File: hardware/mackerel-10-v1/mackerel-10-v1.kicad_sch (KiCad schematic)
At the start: 24 parts, among them J1 Conn_02x05_Odd_Even, U1 68010D, X1 50 MHz

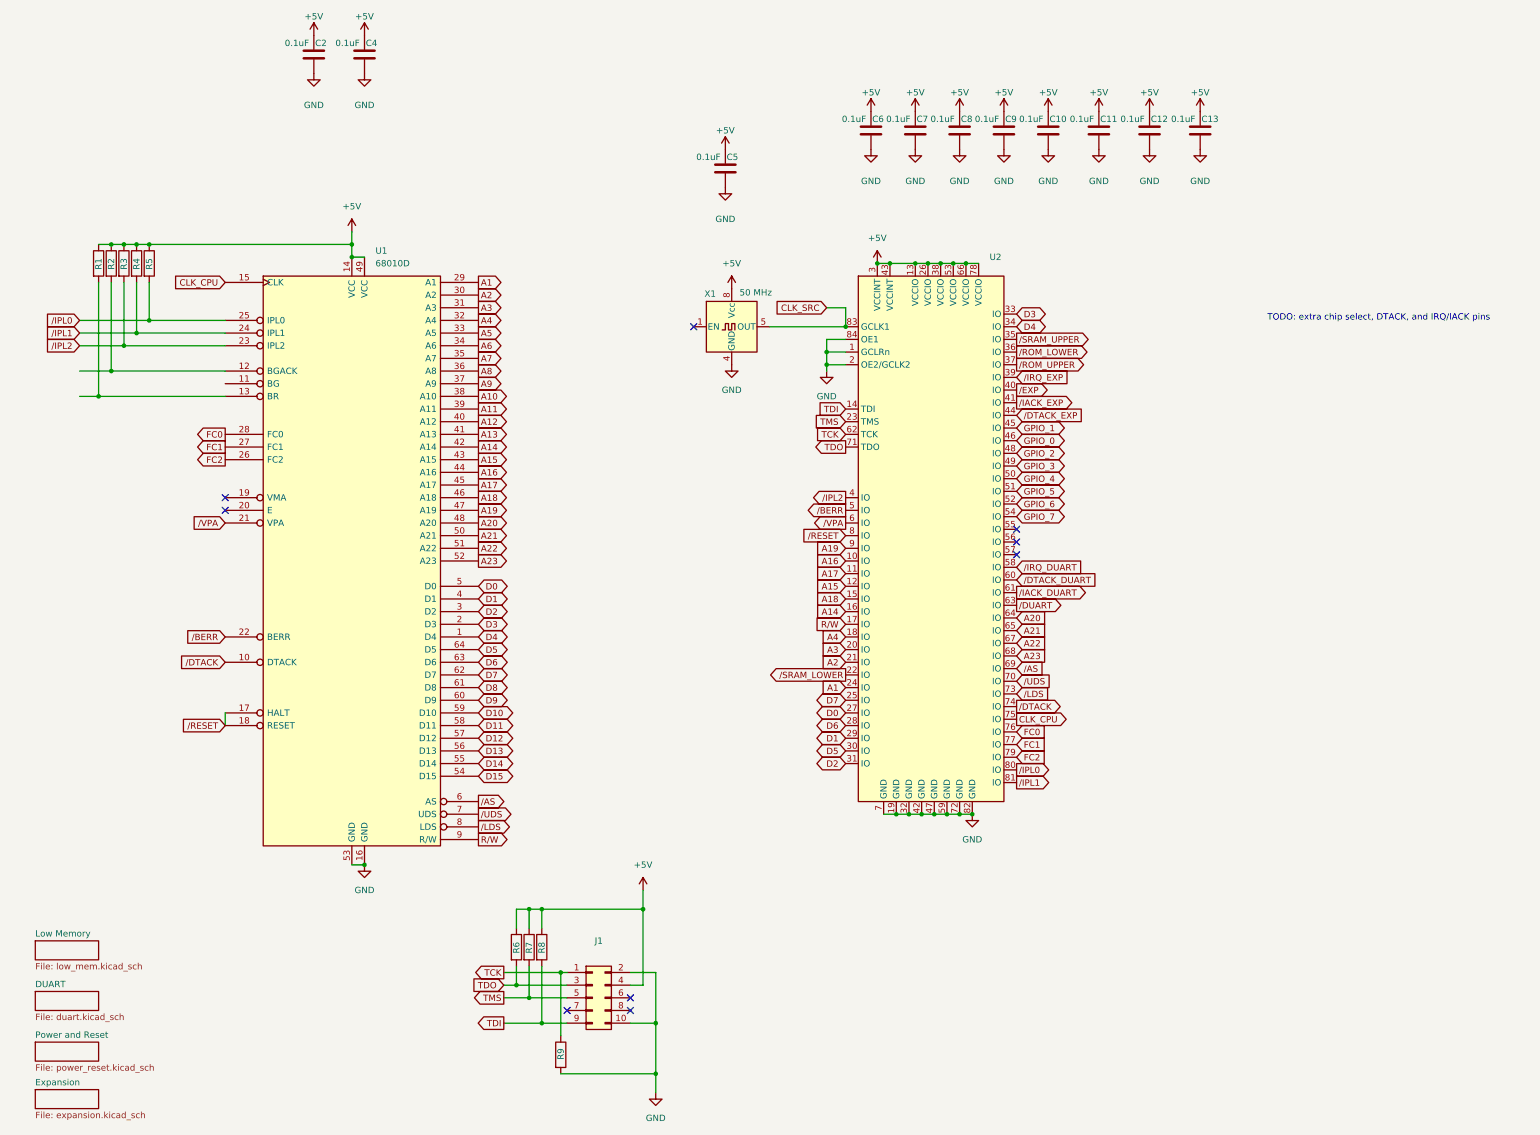
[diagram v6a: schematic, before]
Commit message: Mack-10 proto routed and passing DRC
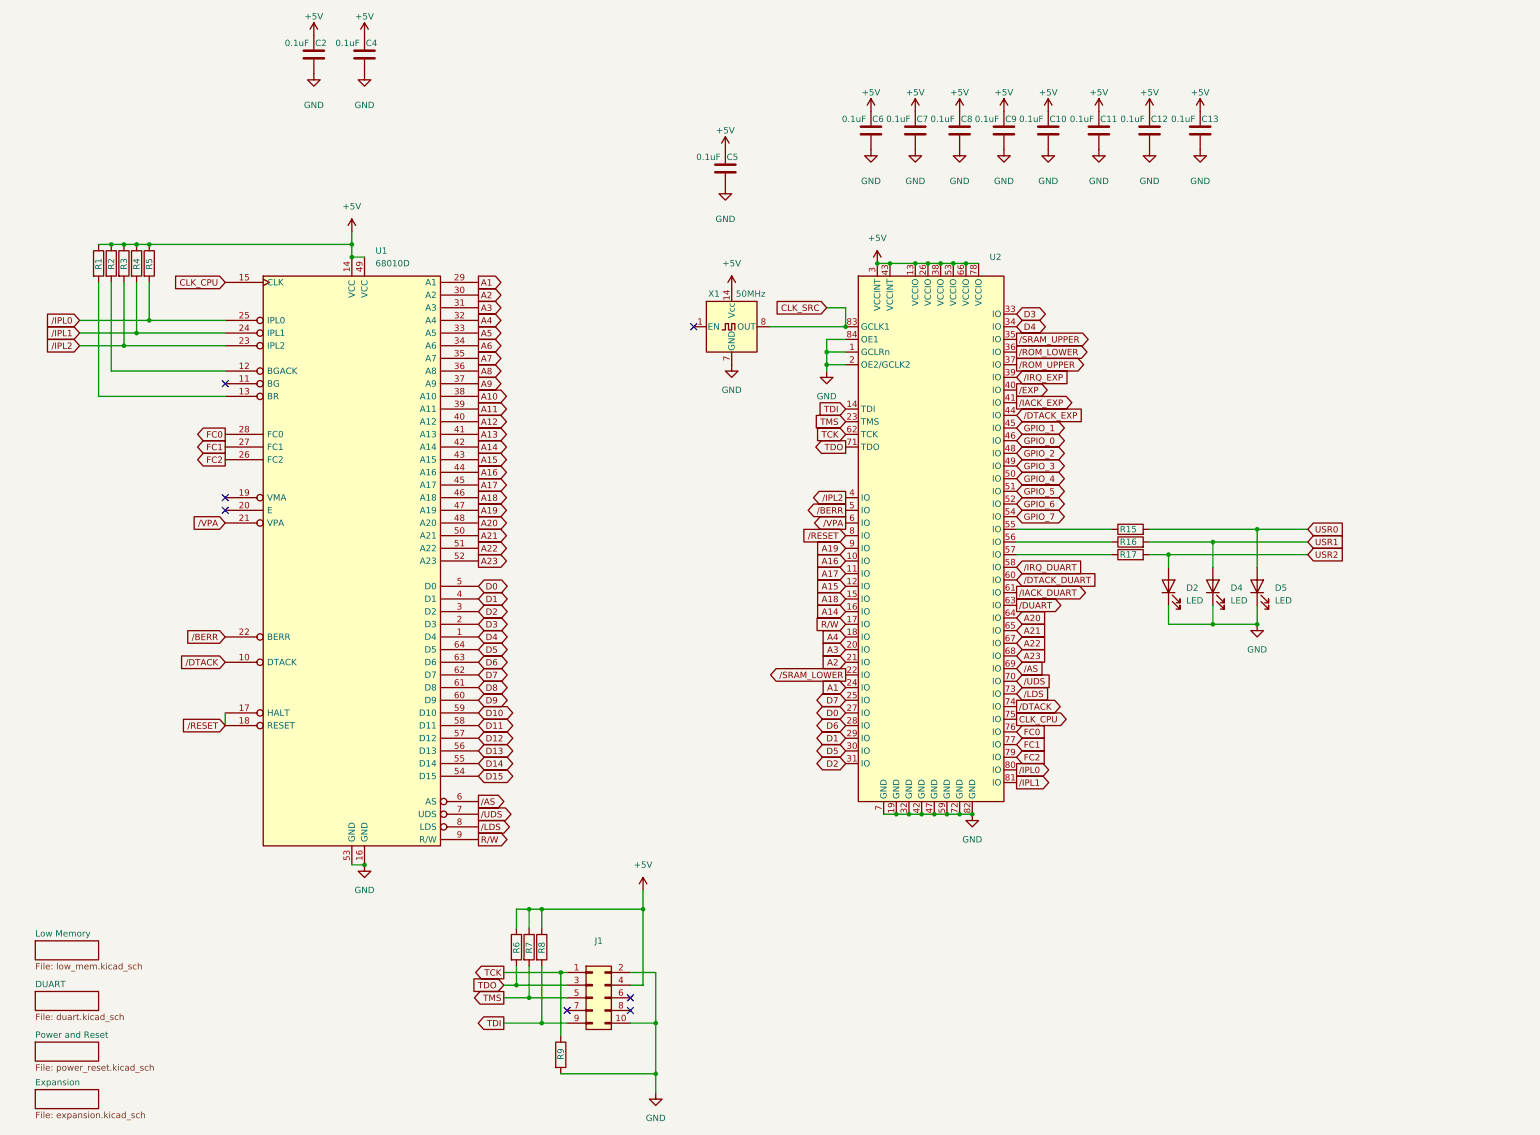
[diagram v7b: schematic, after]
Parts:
- removed X1: 50 MHz, Oscillator:Oscillator_DIP-8, symbol Oscillator:CXO_DIP8
- added D2, D4, D5: LED, LED_THT:LED_D5.0mm, symbol Device:LED
- added R15, R16, R17: R, Resistor_THT:R_Axial_DIN0204_L3.6mm_D1.6mm_P5.08mm_Horizontal, symbol Device:R
- added X1: 50MHz, Oscillator:Oscillator_DIP-14, symbol Oscillator:CXO_DIP14
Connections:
- net +5V: now also X1.14 (Vcc)
- net CLK_SRC: now also X1.8 (OUT)
- net GND: now also D2.1 (K), D4.1 (K), D5.1 (K), X1.7 (GND)
- net at U2.55 (IO): now also R15.1
- net at U2.56 (IO): now also R16.1
- net at U2.57 (IO): now also R17.1
- new net USR0: D5.2 (A), R15.2
- new net USR1: D4.2 (A), R16.2
- new net USR2: D2.2 (A), R17.2
- no-connect marks 9 -> 7
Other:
- note removed: "TODO: extra chip select, DTACK, and IRQ/IACK pins"

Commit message: Mackerel-10 proto board ready for manufacturing
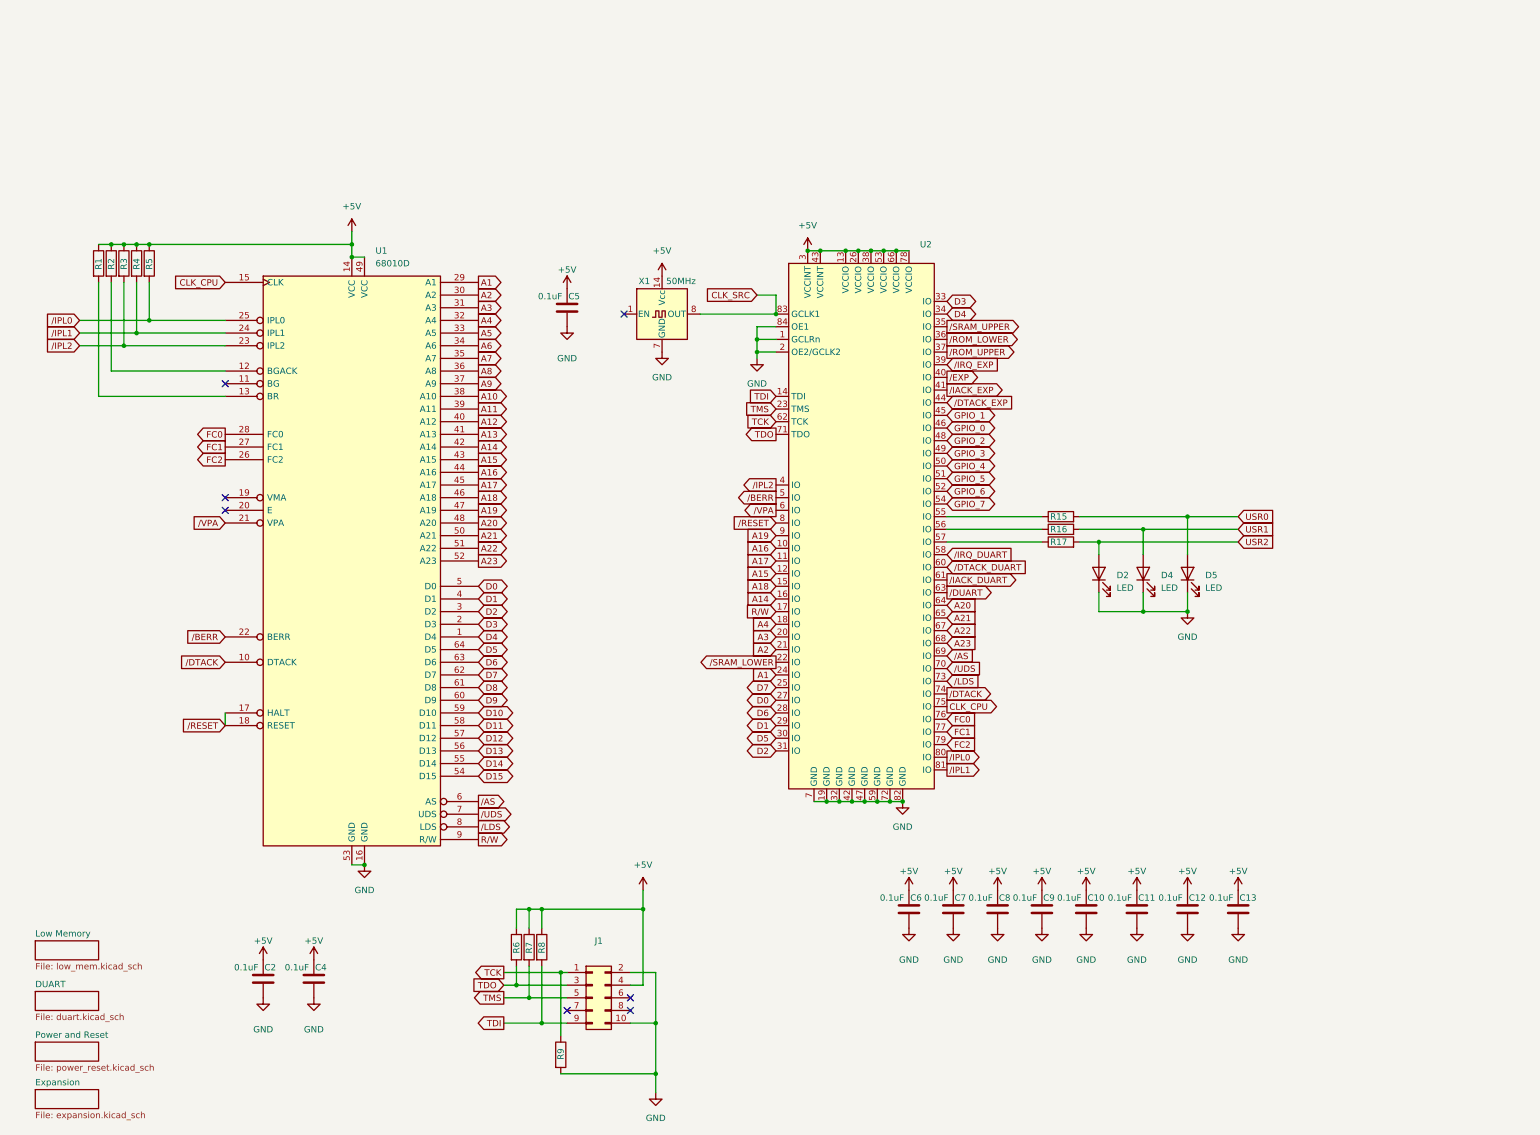
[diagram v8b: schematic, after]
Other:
- moved on the sheet: C10, C11, C12, C13, C2, C4, C5, C6, C7, C8, C9, D2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
